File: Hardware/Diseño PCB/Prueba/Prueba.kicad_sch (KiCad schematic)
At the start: 54 parts, among them J1 Vo, J2 V_Rs_test, J3 V_current_test, J4 V_voltage_test, J5 V_ref_test, J6 V_ref_c_test, Q1 2N3904, Q10 BC557, Q11 BC547, Q12 BC557, Q13 2N3906, Q14 2N3904, Q15 2N3906, Q16 2N3904, Q17 2N3906, Q18 2N3904, Q19 2N3904, Q2 2N3904, Q3 2N3904, Q4 2N3906, Q5 2N3906, Q6 2N3904, Q7 2N3904, Q8 IRF4905, Q9 BC547, U1 TL431LP, U2 LM358, U3 LM358

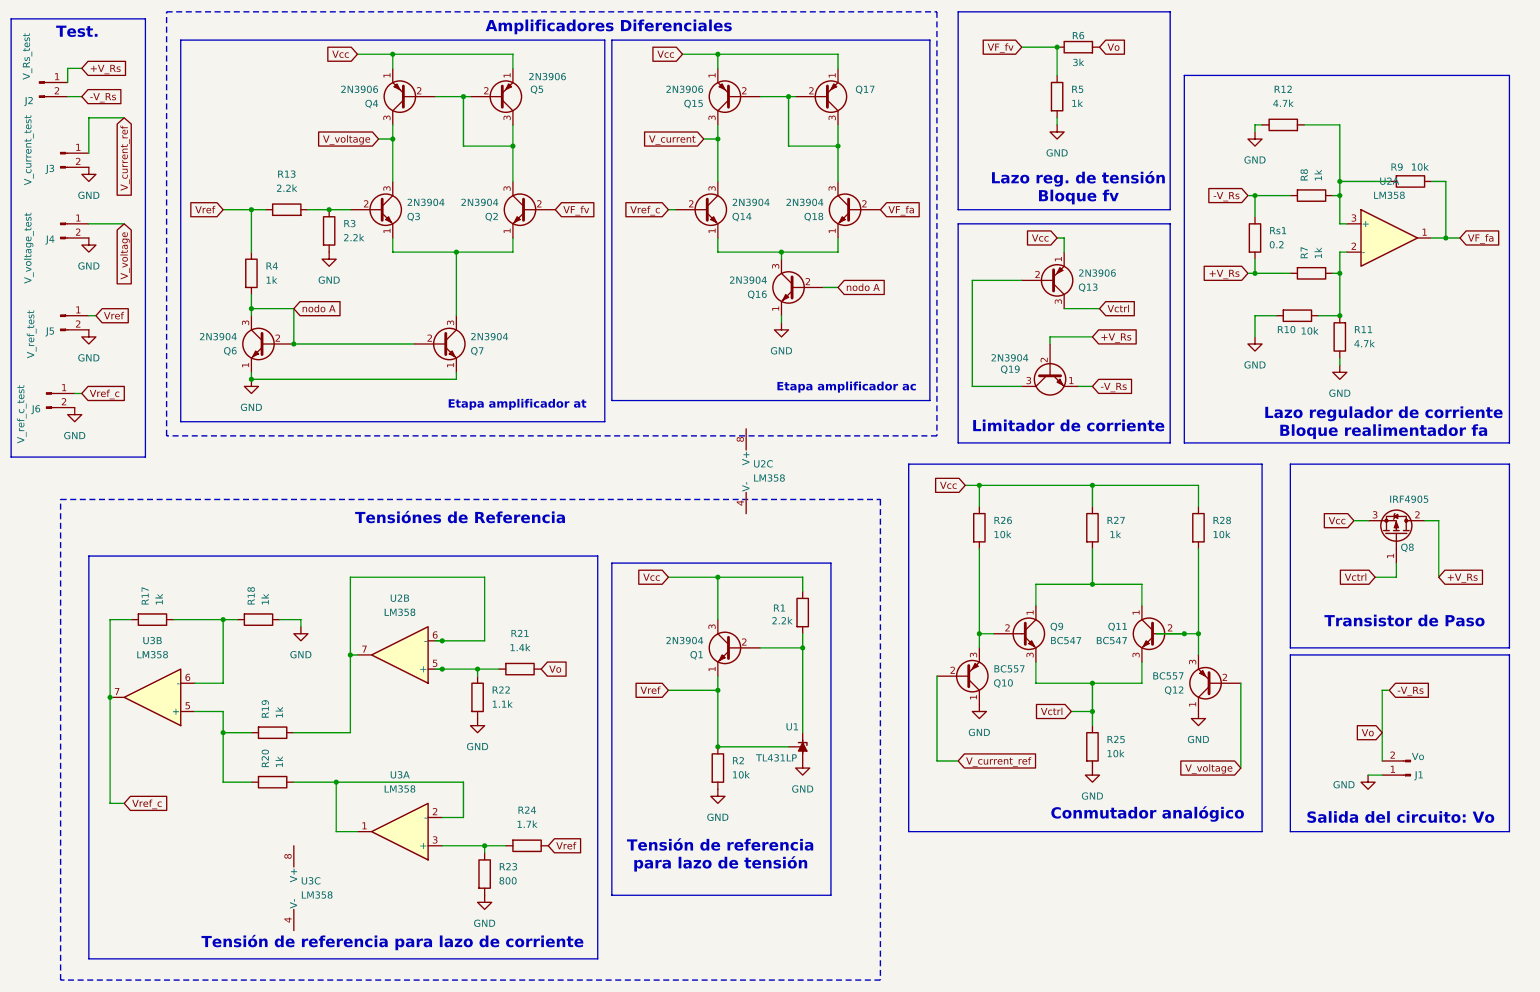
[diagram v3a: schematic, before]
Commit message: LM324 Agregado
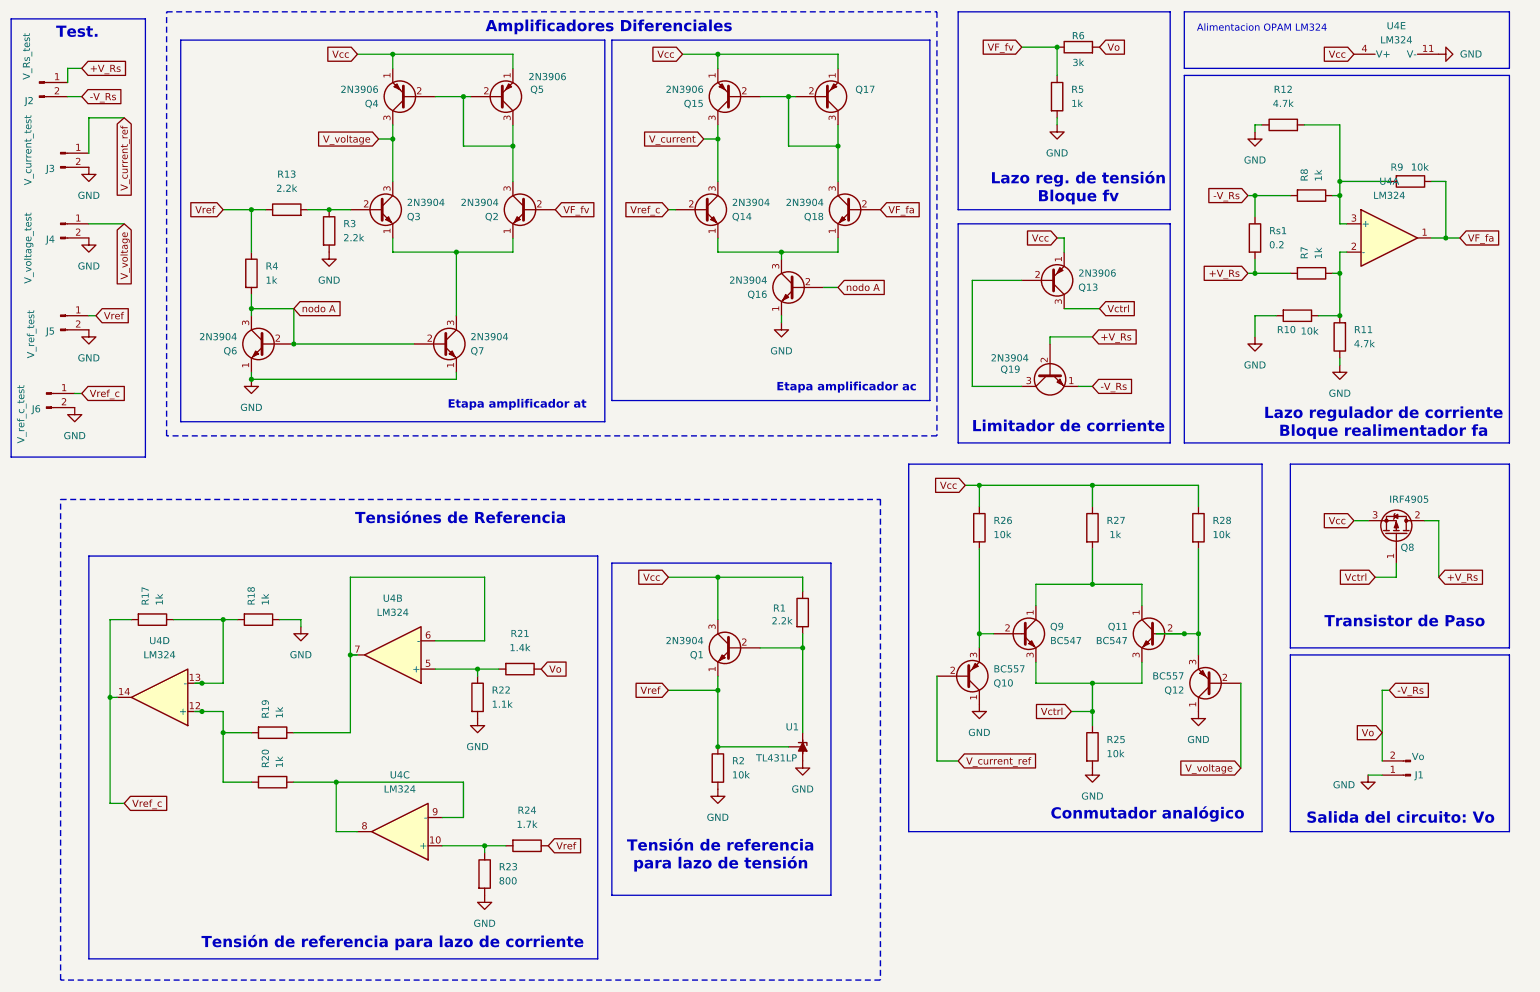
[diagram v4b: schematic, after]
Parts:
- removed U2, U3: LM358, Package_DIP:DIP-8_W7.62mm, symbol Amplifier_Operational:LM358
- added U4: LM324, Package_DIP:DIP-16_W10.16mm_LongPads, symbol Amplifier_Operational:LM324
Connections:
- net GND: now also U4.11 (V-)
- net VF_fa: now also U4.1
- net Vcc: now also U4.4 (V+)
- net Vref_c: now also U4.14
- net at R10.1, R11.2, R7.1: now also U4.2 (-)
- net at R12.2, R8.1, R9.2: now also U4.3 (+)
- net at R20.1: now also U4.8, U4.9 (-)
- net at R23.1, R24.2: now also U4.10 (+)
- net at R21.2, R22.1: now also U4.5 (+)
- net at R19.1: now also U4.6 (-), U4.7
- net at R19.2, R20.2: now also U4.12 (+)
- net at R17.1, R18.2: now also U4.13 (-)
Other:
- note added: "Alimentacion OPAM LM324"

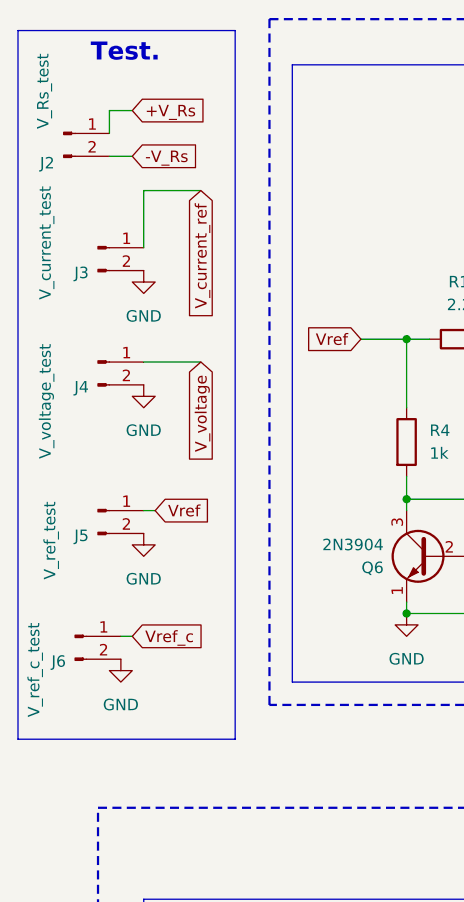
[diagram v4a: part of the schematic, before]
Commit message: Agrupación de modulos en diseño de PCB
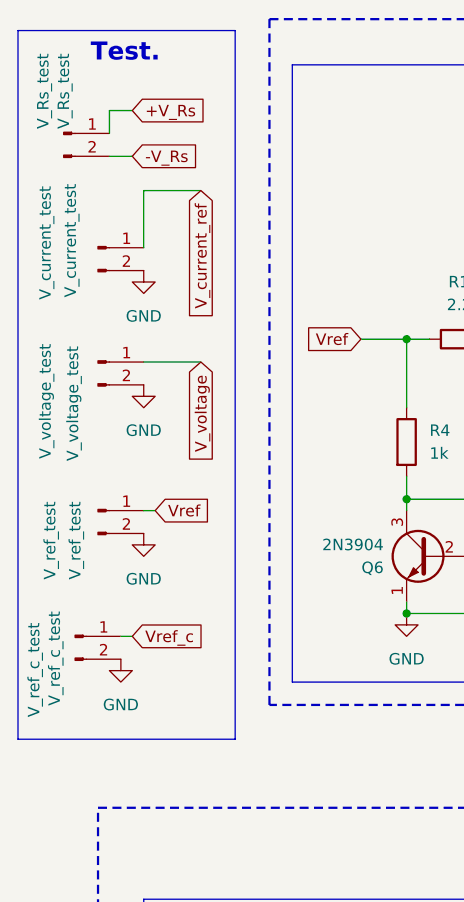
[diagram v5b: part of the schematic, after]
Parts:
- renumbered J2 to V_Rs_test, J3 to V_current_test, J6 to V_ref_c_test, J5 to V_ref_test, J4 to V_voltage_test
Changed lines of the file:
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@@
 		(in_pos_files yes)
 		(dnp no)
-		(property "Reference" "J3"
-			(at 21.844 42.164 0)
+		(property "Reference" "V_current_test"
+			(at 19.812 32.258 90)
 			(show_name no)
 			(do_not_autoplace no)
@@
 			(project "Prueba"
 				(path "/70bda0a3-0c17-43ce-af47-54d014630cec"
-					(reference "J3")
+					(reference "V_current_test")
 					(unit 1)
 				)
@@
 		(in_pos_files yes)
 		(dnp no)
-		(property "Reference" "J4"
-			(at 21.844 54.864 0)
+		(property "Reference" "V_voltage_test"
+			(at 20.066 50.292 90)
 			(show_name no)
 			(do_not_autoplace no)
@@
 			(project "Prueba"
 				(path "/70bda0a3-0c17-43ce-af47-54d014630cec"
-					(reference "J4")
+					(reference "V_voltage_test")
 					(unit 1)
 				)
@@
 		(in_pos_files yes)
 		(dnp no)
-		(property "Reference" "J6"
-			(at 19.304 85.344 0)
+		(property "Reference" "V_ref_c_test"
+			(at 18.034 79.756 90)
 			(show_name no)
 			(do_not_autoplace no)
@@
 			(project "Prueba"
 				(path "/70bda0a3-0c17-43ce-af47-54d014630cec"
-					(reference "J6")
+					(reference "V_ref_c_test")
 					(unit 1)
 				)
@@
 		(in_pos_files yes)
 		(dnp no)
-		(property "Reference" "J2"
-			(at 18.034 29.972 0)
+		(property "Reference" "V_Rs_test"
+			(at 19.05 17.78 90)
 			(show_name no)
 			(do_not_autoplace no)
@@
 			(project "Prueba"
 				(path "/70bda0a3-0c17-43ce-af47-54d014630cec"
-					(reference "J2")
+					(reference "V_Rs_test")
 					(unit 1)
 				)
@@
 		(in_pos_files yes)
 		(dnp no)
-		(property "Reference" "J5"
-			(at 21.844 71.374 0)
+		(property "Reference" "V_ref_test"
+			(at 20.32 67.564 90)
 			(show_name no)
 			(do_not_autoplace no)
@@
 			(project "Prueba"
 				(path "/70bda0a3-0c17-43ce-af47-54d014630cec"
-					(reference "J5")
+					(reference "V_ref_test")
 					(unit 1)
 				)
